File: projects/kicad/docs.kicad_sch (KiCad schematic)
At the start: 20 parts, among them J1 Micro_SD_Card, SW1 SW_PUSH, SW2 SW_PUSH, SW3 SW_PUSH, SW4 SW_PUSH, SW5 SW_PUSH, SW6 SW_PUSH, SW7 RotaryEncoder_Switch, U1 Pico, U2 LCD

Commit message: Update_0122
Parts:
- added LED1: YS-SK6812MINI-E, symbol kbd:YS-SK6812MINI-E
- D1, D2, D3, D4, D5, D6, D7: footprint (none) -> kbd_parts:D_SOD-123-Pretty
- SW1, SW2, SW3, SW4, SW5, SW6: footprint (none) -> kbd:keyswitch_choc12_gateron_low_profile_hotswap_1u_no_led
- SW7: footprint (none) -> Rotary_Encoder:RotaryEncoder_Bourns_Vertical_PEC12R-3x17F-Sxxxx
- U2: footprint (none) -> ST7789v_Library:ST7789V
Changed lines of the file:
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@@
 			)
 		)
-		(property "Footprint" ""
+		(property "Footprint" "kbd:keyswitch_choc12_gateron_low_profile_hotswap_1u_no_led"
 			(at 177.8 39.37 0)
 			(effects
@@
 			)
 		)
-		(property "Footprint" ""
+		(property "Footprint" "ST7789v_Library:ST7789V"
 			(at 153.67 123.19 0)
 			(effects
@@
 			)
 		)
-		(property "Footprint" ""
+		(property "Footprint" "kbd_parts:D_SOD-123-Pretty"
 			(at 139.7 83.82 0)
 			(effects
@@
 			)
 		)
-		(property "Footprint" ""
+		(property "Footprint" "kbd_parts:D_SOD-123-Pretty"
 			(at 167.64 63.5 0)
 			(effects
@@
 			)
 		)
-		(property "Footprint" ""
+		(property "Footprint" "kbd_parts:D_SOD-123-Pretty"
 			(at 139.7 44.45 0)
 			(effects
@@
 			)
 		)
-		(property "Footprint" ""
+		(property "Footprint" "kbd:keyswitch_choc12_gateron_low_profile_hotswap_1u_no_led"
 			(at 177.8 57.15 0)
 			(effects
@@
 			)
 		)
-		(property "Footprint" ""
+		(property "Footprint" "Rotary_Encoder:RotaryEncoder_Bourns_Vertical_PEC12R-3x17F-Sxxxx"
 			(at 173.99 96.266 0)
 			(effects
@@
 				(path "/eb9efe38-c1c1-4280-ba2b-08a47c3e2531"
 					(reference "SW7")
+					(unit 1)
+				)
+			)
+		)
+	)
+	(symbol
+		(lib_id "kbd:YS-SK6812MINI-E")
+		(at 101.6 26.67 0)
+		(unit 1)
+		(exclude_from_sim no)
+		(in_bom yes)
+		(on_board yes)
+		(dnp no)
+		(fields_autoplaced yes)
+		(property "Reference" "LED1"
+			(at 113.03 22.2565 0)
+			(effects
+				(font
+					(size 0.7366 0.7366)
+				)
+			)
+		)
+		(property "Value" "YS-SK6812MINI-E"
+			(at 113.03 23.5265 0)
+			(effects
+				(font
+					(size 0.7366 0.7366)
+				)
+			)
+		)
+		(property "Footprint" ""
+			(at 104.14 33.02 0)
+			(effects
+				(font
+					(size 1.27 1.27)
+				)
+				(hide yes)
+			)
+		)
+		(property "Datasheet" ""
+			(at 104.14 33.02 0)
+			(effects
+				(font
+					(size 1.27 1.27)
+				)
+				(hide yes)
+			)
+		)
+		(property "Description" ""
+			(at 101.6 26.67 0)
+			(effects
+				(font
+					(size 1.27 1.27)
+				)
+				(hide yes)
+			)
+		)
+		(pin "4"
+		)
+		(pin "2"
+		)
+		(pin "1"
+		)
+		(pin "3"
+		)
+		(instances
+			(project ""
+				(path "/eb9efe38-c1c1-4280-ba2b-08a47c3e2531"
+					(reference "LED1")
 					(unit 1)
 				)
@@
 			)
 		)
-		(property "Footprint" ""
+		(property "Footprint" "kbd_parts:D_SOD-123-Pretty"
 			(at 187.96 107.95 0)
 			(effects
@@
 			)
 		)
-		(property "Footprint" ""
+		(property "Footprint" "kbd_parts:D_SOD-123-Pretty"
 			(at 167.64 44.45 0)
 			(effects
@@
 			)
 		)
-		(property "Footprint" ""
+		(property "Footprint" "kbd_parts:D_SOD-123-Pretty"
 			(at 167.64 83.82 0)
 			(effects
@@
 			)
 		)
-		(property "Footprint" ""
+		(property "Footprint" "kbd:keyswitch_choc12_gateron_low_profile_hotswap_1u_no_led"
 			(at 151.13 76.2 0)
 			(effects
@@
 			)
 		)
-		(property "Footprint" ""
+		(property "Footprint" "kbd:keyswitch_choc12_gateron_low_profile_hotswap_1u_no_led"
 			(at 151.13 57.15 0)
 			(effects
@@
 			)
 		)
-		(property "Footprint" ""
+		(property "Footprint" "kbd:keyswitch_choc12_gateron_low_profile_hotswap_1u_no_led"
 			(at 151.13 39.37 0)
 			(effects
@@
 			)
 		)
-		(property "Footprint" ""
+		(property "Footprint" "kbd:keyswitch_choc12_gateron_low_profile_hotswap_1u_no_led"
 			(at 177.8 76.2 0)
 			(effects
@@
 			)
 		)
-		(property "Footprint" ""
+		(property "Footprint" "kbd_parts:D_SOD-123-Pretty"
 			(at 139.7 63.5 0)
 			(effects

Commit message: chocolate: Update_0126
TFTディスプレイ 240x320 追加
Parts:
- D10, D8, D9: footprint (none) -> kbd:LED_WS2812B-PLCC4
- U2: footprint ST7789v_Library:ST7789V -> tft_displays:2.8_tft_240x320_touch_sd_spi
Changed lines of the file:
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@@
 			)
 		)
-		(property "Footprint" ""
+		(property "Footprint" "kbd:LED_WS2812B-PLCC4"
 			(at 24.13 55.88 0)
 			(effects
@@
 			)
 		)
-		(property "Footprint" "ST7789v_Library:ST7789V"
+		(property "Footprint" "tft_displays:2.8_tft_240x320_touch_sd_spi"
 			(at 153.67 123.19 0)
 			(effects
@@
 			)
 		)
-		(property "Footprint" ""
+		(property "Footprint" "kbd:LED_WS2812B-PLCC4"
 			(at 24.13 35.56 0)
 			(effects
@@
 			)
 		)
-		(property "Footprint" ""
+		(property "Footprint" "kbd:LED_WS2812B-PLCC4"
 			(at 24.13 45.72 0)
 			(effects

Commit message: Update_0128
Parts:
- removed J1: Micro_SD_Card, symbol Connector:Micro_SD_Card
- removed LED1: YS-SK6812MINI-E, symbol kbd:YS-SK6812MINI-E
- removed U2: LCD, tft_displays:2.8_tft_240x320_touch_sd_spi, symbol 4xxx_IEEE:4001
- added U3: 2.8_240x320_touch_sd_spi, original_tft_display:2.8_tft_240x320_touch_sd_spi, symbol TFT Displays:2.8_240x320_touch_sd_spi
- U1: footprint RPi_Pico:RPi_Pico_SMD_TH -> KiCad-RP-Pico-main:RPi_Pico_SMD_TH
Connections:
- net 3V3 Out: now also U3.1 (VCC)
- net CS: now also U3.3 (CS)
- net DC: now also U3.5 (D/C)
- net GND: now also U3.2 (GND)
- net RST: now also U3.4 (RESET)
- net SCL: now also U3.7 (SCK)
- net SDA: now also U3.9 (SDO(MISO))

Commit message: Update_0129
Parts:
- removed D10, D8, D9: LED, kbd:LED_WS2812B-PLCC4, symbol Device:LED
- added LED1, LED2, LED3: YS-SK6812MINI-E, kbd:YS-SK6812MINI-E, symbol kbd:YS-SK6812MINI-E
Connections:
- net 3V3 Out: now also LED1.1 (VDD), LED2.1 (VDD), LED3.1 (VDD)
- net GND: now also LED1.3 (VSS), LED2.3 (VSS), LED3.3 (VSS)
- net SCL: now also U1.32 (GPIO27_ADC1); no longer U1.31 (GPIO26_ADC0)
- net SDA: now also U1.31 (GPIO26_ADC0); no longer U1.32 (GPIO27_ADC1)
- net LED: now reaches U1.5 (GPIO3)
- net LED: now also LED1.4 (DIN)
- new net: LED2.2 (DOUT), LED3.4 (DIN)
- new net: LED1.2 (DOUT), LED2.4 (DIN)
- no-connect marks 0 -> 28
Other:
- moved on the sheet: U1

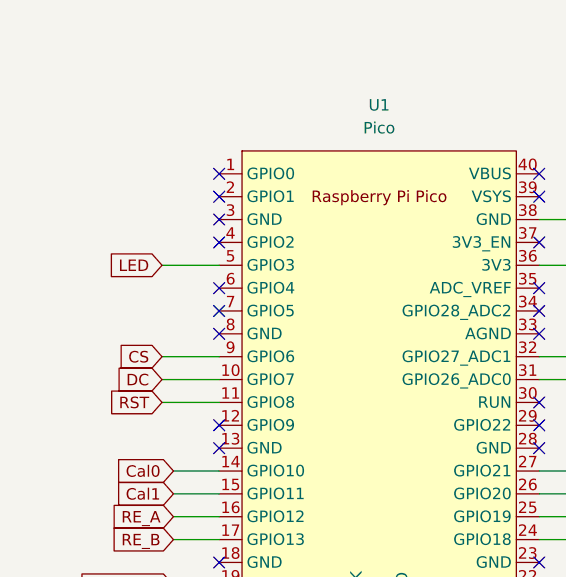
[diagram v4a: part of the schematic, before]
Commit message: chocolate: 配線図を整理
配線整理に合わせて回路図も一部修正
PCBのデザインルールチェッカーで確認済み：エラー12件
(LEDに関するものでフットプリント時からあり？)
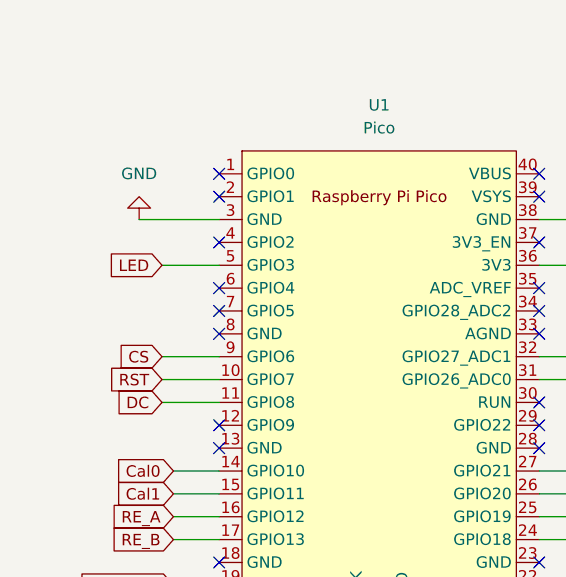
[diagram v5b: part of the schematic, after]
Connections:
- net DC: now also U1.11 (GPIO8); no longer U1.10 (GPIO7)
- net GND: now also U1.3 (GND)
- net RST: now also U1.10 (GPIO7); no longer U1.11 (GPIO8)
- no-connect marks 28 -> 27
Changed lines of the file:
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@@
-	)
-	(no_connect
-		(at 69.85 44.45)
 	)
 	(no_connect
@@
 	(wire
 		(pts
+			(xy 63.5 64.77) (xy 69.85 64.77)
+		)
+		(stroke
+			(width 0)
+			(type default)
+		)
+	)
+	(wire
+		(pts
 			(xy 105.41 80.01) (xy 110.49 80.01)
 		)
@@
 	(wire
 		(pts
-			(xy 63.5 64.77) (xy 69.85 64.77)
-		)
-		(stroke
-			(width 0)
-			(type default)
-		)
-	)
-	(wire
-		(pts
 			(xy 105.41 77.47) (xy 110.49 77.47)
 		)
@@
 	(wire
 		(pts
+			(xy 60.96 44.45) (xy 69.85 44.45)
+		)
+		(stroke
+			(width 0)
+			(type default)
+		)
+	)
+	(wire
+		(pts
 			(xy 167.64 57.15) (xy 167.64 59.69)
 		)
@@
 	(wire
 		(pts
+			(xy 63.5 62.23) (xy 69.85 62.23)
+		)
+		(stroke
+			(width 0)
+			(type default)
+		)
+	)
+	(wire
+		(pts
 			(xy 64.77 72.39) (xy 69.85 72.39)
 		)
@@
 	(wire
 		(pts
-			(xy 63.5 62.23) (xy 69.85 62.23)
-		)
-		(stroke
-			(width 0)
-			(type default)
-		)
-	)
-	(wire
-		(pts
 			(xy 139.7 67.31) (xy 167.64 67.31)
 		)
@@
 	(global_label "RST"
 		(shape input)
+		(at 63.5 62.23 180)
+		(fields_autoplaced yes)
+		(effects
+			(font
+				(size 1.27 1.27)
+			)
+			(justify right)
+		)
+		(property "Intersheetrefs" "${INTERSHEET_REFS}"
+			(at 57.0677 62.23 0)
+			(effects
+				(font
+					(size 1.27 1.27)
+				)
+				(justify right)
+				(hide yes)
+			)
+		)
+	)
+	(global_label "Row0"
+		(shape input)
+		(at 110.49 72.39 0)
+		(fields_autoplaced yes)
+		(effects
+			(font
+				(size 1.27 1.27)
+			)
+			(justify left)
+		)
+		(property "Intersheetrefs" "${INTERSHEET_REFS}"
+			(at 118.4342 72.39 0)
+			(effects
+				(font
+					(size 1.27 1.27)
+				)
+				(justify left)
+				(hide yes)
+			)
+		)
+	)
+	(global_label "3V3 Out"
+		(shape input)
+		(at 109.22 49.53 0)
+		(fields_autoplaced yes)
+		(effects
+			(font
+				(size 1.27 1.27)
+			)
+			(justify left)
+		)
+		(property "Intersheetrefs" "${INTERSHEET_REFS}"
+			(at 119.8856 49.53 0)
+			(effects
+				(font
+					(size 1.27 1.27)
+				)
+				(justify left)
+				(hide yes)
+			)
+		)
+	)
+	(global_label "DC"
+		(shape input)
 		(at 63.5 64.77 180)
 		(fields_autoplaced yes)
@@
 		)
 		(property "Intersheetrefs" "${INTERSHEET_REFS}"
-			(at 57.0677 64.77 0)
-			(effects
-				(font
-					(size 1.27 1.27)
-				)
-				(justify right)
-				(hide yes)
-			)
-		)
-	)
-	(global_label "Row0"
-		(shape input)
-		(at 110.49 72.39 0)
-		(fields_autoplaced yes)
-		(effects
-			(font
-				(size 1.27 1.27)
-			)
-			(justify left)
-		)
-		(property "Intersheetrefs" "${INTERSHEET_REFS}"
-			(at 118.4342 72.39 0)
-			(effects
-				(font
-					(size 1.27 1.27)
-				)
-				(justify left)
-				(hide yes)
-			)
-		)
-	)
-	(global_label "3V3 Out"
-		(shape input)
-		(at 109.22 49.53 0)
-		(fields_autoplaced yes)
-		(effects
-			(font
-				(size 1.27 1.27)
-			)
-			(justify left)
-		)
-		(property "Intersheetrefs" "${INTERSHEET_REFS}"
-			(at 119.8856 49.53 0)
-			(effects
-				(font
-					(size 1.27 1.27)
-				)
-				(justify left)
-				(hide yes)
-			)
-		)
-	)
-	(global_label "DC"
-		(shape input)
-		(at 63.5 62.23 180)
-		(fields_autoplaced yes)
-		(effects
-			(font
-				(size 1.27 1.27)
-			)
-			(justify right)
-		)
-		(property "Intersheetrefs" "${INTERSHEET_REFS}"
-			(at 57.9748 62.23 0)
+			(at 57.9748 64.77 0)
 			(effects
 				(font
@@
 					(unit 1)
 				)
+			)
+		)
+	)
+	(symbol
+		(lib_id "power:GND")
+		(at 60.96 44.45 180)
+		(unit 1)
+		(exclude_from_sim no)
+		(in_bom yes)
+		(on_board yes)
+		(dnp no)
+		(fields_autoplaced yes)
+		(property "Reference" "#PWR03"
+			(at 60.96 38.1 0)
+			(effects
+				(font
+					(size 1.27 1.27)
+				)
+				(hide yes)
+			)
+		)
+		(property "Value" "GND"
+			(at 60.96 39.37 0)
+			(effects
+				(font
+					(size 1.27 1.27)
+				)
+			)
+		)
+		(property "Footprint" ""
+			(at 60.96 44.45 0)
+			(effects
+				(font
+					(size 1.27 1.27)
+				)
+				(hide yes)
+			)
+		)
+		(property "Datasheet" ""
+			(at 60.96 44.45 0)
+			(effects
+				(font
+					(size 1.27 1.27)
+				)
+				(hide yes)
+			)
+		)
+		(property "Description" "Power symbol creates a global label with name \"GND\" , ground"
+			(at 60.96 44.45 0)
+			(effects
+				(font
+					(size 1.27 1.27)
+				)
+				(hide yes)
+			)
+		)
+		(pin "1"
+		)
+		(instances
+			(project ""
+				(path "/eb9efe38-c1c1-4280-ba2b-08a47c3e2531"
+					(reference "#PWR03")
+					(unit 1)
+				)
